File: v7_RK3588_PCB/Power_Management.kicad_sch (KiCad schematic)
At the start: 0 parts

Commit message: add symbols
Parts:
- added U3001: ~, RK806-1:QFN-68_L7.0-W7.0-P0.35-BL-EP5.5, symbol RK806-1:RK806-1_C5156483

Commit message: add regulators
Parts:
- added C3001, C3012, C3013: 47u, symbol Device:C
- added C3002, C3003: 22u, symbol Device:C
- added C3004, C3005: 10u, symbol Device:C
- added C3006, C3014: 100n, symbol Device:C
- added C3007, C3008: 1u, symbol Device:C
- added C3009: 47p, symbol Device:C
- added C3010: 1n, symbol Device:C
- added C3011: 8.2n, symbol Device:C
- added L3001: 220n, symbol Device:L
- added L3002: 1u, symbol Device:L
- added R3001: 100k, symbol Device:R
- added R3002: 205k, symbol Device:R
- added R3003: 23.7k, symbol Device:R
- added R3004: 124k, symbol Device:R
- added R3005: 267k, symbol Device:R
- added R3006: 220k, symbol Device:R
- added R3007: 69.8k, symbol Device:R
- added U3002: TPS62867RQYR, TPS62867RQYR:RQY0009A-MFG, symbol TPS62867RQYR:TPS62867RQYR
- added U3003: TPS61088RHLR, TPS61088RHLR:IC_TPS61088RHLR, symbol TPS61088RHLR:TPS61088RHLR
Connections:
- new net: C3004.1, C3005.1, C3006.1, L3002.1, U3003.9 (VIN)
- new net: R3006.2, R3007.1, U3003.17 (FB)
- new net: C3007.1, C3008.1, U3003.1 (VCC)
- new net: C3014.2, L3002.2, R3005.1, U3003.4 (SW_7), U3003.5 (SW_4), U3003.6 (SW_5), U3003.7 (SW_6)
- new net: R3005.2, U3003.3 (FSW)
- new net: C3009.1, R3003.1, U3003.18 (COMP)
- new net: R3002.1, U3002.6 (VSET_MODE)
- new net: C3014.1, U3003.8 (BOOT)
- new net: L3001.1, U3002.7 (SW)
- new net: C3010.1, R3003.2
- new net: R3004.1, U3003.19 (ILIM)
- new net: C3011.1, U3003.10 (SS)
- new net 5V0_OUT_ETH: C3001.1, R3001.1, U3002.3 (VIN), U3002.4 (EN)
- new net BAT_5V: C3012.1, C3013.1, R3006.1, U3003.14 (VOUT_16), U3003.15 (VOUT_14), U3003.16 (VOUT_15)
- new net ETH_3V3: C3002.1, C3003.1, L3001.2, U3002.8 (VOS), U3002.9 (FB)
- new net ETH_3V3_PG: R3001.2, U3002.5 (PG)
- new net GND: C3001.2, C3002.2, C3003.2, C3004.2, C3005.2, C3006.2, C3007.2, C3008.2, C3009.2, C3010.2, C3011.2, C3012.2, C3013.2, R3002.2, R3004.2, R3007.2, U3002.1 (AGND), U3002.2 (PGND), U3003.11 (NC_11), U3003.20 (AGND), U3003.21 (PGND), U3003.22 (PGND__1), U3003.23 (PGND__2), U3003.24 (PGND__3), U3003.25 (PGND__4), U3003.26 (PGND__5), U3003.27 (PGND__6), U3003.28 (PGND__7), U3003.29 (PGND__8)
- no-connect marks 0 -> 1
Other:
- note added: "Battery to 5V"
- note added: "CONNECT TO IDEAL DIODE PG"
- note added: "PoE to 3.3V"
- note added: "SEE PG 12 OF DATASHEET FOR CAP. VALUE CALC"
- note added: "USE PG TO DISABLE BATTERY 3V3 REG"
- moved on the sheet: U3001

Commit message: add battery management
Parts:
- added BT3001, BT3002: Battery_Cell, symbol Device:Battery_Cell
- added C3015, C3016, C3017, C3018: 0.1u, symbol Device:C
- added C3019, C3020: 4.3n, symbol Device:C
- added R3008, R3015: 470k, symbol Device:R
- added R3009, R3017: 118k, symbol Device:R
- added R3010, R3020: 215k, symbol Device:R
- added R3011, R3021: 576, symbol Device:R
- added R3012, R3016: 47k, symbol Device:R
- added R3013, R3018: 27.4k, symbol Device:R
- added R3014, R3019: 10k, symbol Device:R
- added U3004, U3005: LTC4450AV-TRMPBF, LTC4450:05-08-1683_ADI, symbol LTC4450:LTC4450AV-TRMPBF
- added U3006, U3007: TPS22811LRPWR, TPS22811LRPWR:IC_TPS22811LRPWR, symbol TPS22811LRPWR:TPS22811LRPWR
- added U3008: SN74AHC1G32DCKR, SN74AHC1G32DCKR:SOT65P210X110-5N, symbol SN74AHC1G32DCKR:SN74AHC1G32DCKR
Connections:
- net GND: now also BT3001.2 (-), BT3002.2 (-), C3015.2, C3016.2, C3017.2, C3018.2, C3019.2, C3020.2, R3010.2, R3011.2, R3013.2, R3018.2, R3020.2, R3021.2, U3004.1 (VCC), U3004.14 (GND), U3004.15 (STATUS), U3005.1 (VCC), U3005.14 (GND), U3005.15 (STATUS), U3006.8 (GND), U3007.8 (GND), U3008.3 (GND)
- new net: BT3001.1 (+), R3008.1, U3006.5 (IN)
- new net: R3008.2, R3009.1, U3006.1 (EN/UVLO)
- new net: BT3002.1 (+), R3015.1, U3007.5 (IN)
- new net: R3015.2, R3017.1, U3007.1 (EN/UVLO)
- new net: R3009.2, R3010.1, U3006.2 (~{EN}/OVLO)
- new net: R3016.2, R3018.1, U3007.4 (PGTH)
- new net: R3021.1, U3007.9 (IMON)
- new net: C3019.1, U3006.7 (DVDT)
- new net: R3017.2, R3020.1, U3007.2 (~{EN}/OVLO)
- new net: C3020.1, U3007.7 (DVDT)
- new net: R3012.2, R3013.1, U3006.4 (PGTH)
- new net: R3011.1, U3006.9 (IMON)
- new net BATTERY_IN: C3016.1, C3018.1, U3004.10 (OUT), U3004.11 (OUT), U3004.12 (OUT), U3004.13 (OUT), U3004.8 (OUT), U3004.9 (OUT), U3005.10 (OUT), U3005.11 (OUT), U3005.12 (OUT), U3005.13 (OUT), U3005.8 (OUT), U3005.9 (OUT), U3008.5 (VCC)
- new net BATTERY_PG: U3008.4 (Y)
- new net LOAD_OUT_1: C3015.1, R3012.1, U3004.16 (SHDN#), U3004.2 (IN), U3004.3 (IN), U3004.4 (IN), U3004.5 (IN), U3004.6 (IN), U3004.7 (IN), U3006.6 (OUT)
- new net LOAD_OUT_2: C3017.1, R3016.1, U3005.16 (SHDN#), U3005.2 (IN), U3005.3 (IN), U3005.4 (IN), U3005.5 (IN), U3005.6 (IN), U3005.7 (IN), U3007.6 (OUT)
- new net LOAD_PG_1: R3014.2, U3006.3 (PG), U3008.1 (A)
- new net LOAD_PG_2: R3019.2, U3007.3 (PG), U3008.2 (B)
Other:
- note added: "Battery Management"
- note added: "CONNECT TO LOAD SWITCH PG"
- note added: "POSSIBLY ADD INPUT TVS DIODES"
- note added: "STATUS indication unused"
- note added: "TODO: Pull up"
- note added: "TODO: pick and insert fuel gauge"
- note removed: "CONNECT TO IDEAL DIODE PG"
- moved on the sheet: C3001, C3002, C3003, C3004, C3005, C3006, C3007, C3008, C3009, C3010, C3011, C3012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

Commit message: add ESP32 schematic
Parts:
- added R3022: 10k, symbol Device:R
- renumbered C3002 to C3001, C3003 to C3002, C3001 to C3003, C3014 to C3004, C3015 to C3005, C3016 to C3006, C3004 to C3007, C3005 to C3008, C3006 to C3009, C3007 to C3010, C3008 to C3011, C3019 to C3012, C3012 to C3013, C3013 to C3014, C3009 to C3015, C3010 to C3016, C3011 to C3019, R3005 to R3003, R3008 to R3004, R3012 to R3005, R3009 to R3006, R3013 to R3007, R3014 to R3008, R3010 to R3009, R3011 to R3010, R3006 to R3011, R3003 to R3012, R3007 to R3013, R3004 to R3014, U3002 to U3001, U3004 to U3002, U3006 to U3003, U3003 to U3004, U3007 to U3006, U3008 to U3007, U3001 to U3008
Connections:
- net BATTERY_PG: now also U3004.2 (EN)
- net GND: now also U3008.69 (PAD)
- net PMIC_INT_L: now reaches U3008.19 (INT)
- net PMIC_INT_L: now also R3022.2
- net PMIC_EXT_EN_OUT: now reaches U3008.39 (EXT_EN)
- net RESET_L: now reaches U3008.40 (RESETB)
- net PMIC_PWR_CTRL2: now reaches U3008.61 (PWRCRTL2)
- net PMIC_PWR_CTRL1: now reaches U3008.62 (PWRCRTL1)
- new net VCC_1V8_S3: R3022.1
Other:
- note added: "TODO: add another protection IC?"
- note removed: "CONNECT TO LOAD SWITCH PG"
- moved on the sheet: C3004, C3005, C3006, C3007, C3008, C3009, C3010, C3011, C3012, C3013, C3014, C3015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

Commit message: add power sequencing
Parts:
- removed U3007: SN74AHC1G32DCKR, SN74AHC1G32DCKR:SOT65P210X110-5N, symbol SN74AHC1G32DCKR:SN74AHC1G32DCKR
- added C3021, C3022, C3023, C3024, C3025: 0.1u, symbol Device:C
- added R3023, R3024, R3029, R3030: 100, symbol Device:R
- added R3025: 1m, symbol Device:R
- added R3026: 10, symbol Device:R
- added R3027, R3028: 1k, symbol Device:R
- added TH3001: ERT-J0EG103FA, symbol Device:Thermistor
- added U3004: BQ27Z561YPHR-R2, BQ27Z561-R2:DSBGA_YPHR-R2_TEX, symbol BQ27Z561-R2:BQ27Z561YPHR-R2
- added U3008: SN74LVC1G32DBVR, SN74LVC1G32DBVR:SOT95P280X145-5N, symbol SN74LVC1G32DBVR:SN74LVC1G32DBVR
- added U3010: LTC4450AV-TRMPBF, LTC4450:05-08-1683_ADI, symbol LTC4450:LTC4450AV-TRMPBF
- added U3011: SN74LVC1G14DBVR, SN74LVC1G14DBVR:SOT95P280X145-5N, symbol SN74LVC1G14DBVR:SN74LVC1G14DBVR
- added U3012: SN74LVC1G08DBVR, SN74LVC1G08DBVR:SOT95P280X145-5N, symbol SN74LVC1G08DBVR:SN74LVC1G08DBVR
- R3006, R3017: value 118k -> 82.5k
- R3009, R3020: value 215k -> 205k
- renumbered U3004 to U3005, U3005 to U3006, U3006 to U3007, U3008 to U3009
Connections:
- net BATTERY_IN: now also C3021.1, R3024.1, R3025.2, R3026.2, R3027.2, R3028.2, U3008.5 (VCC)
- net BATTERY_PG: now also U3008.4, U3012.2 (B)
- net ETH_3V3: now also C3024.1, U3010.16 (SHDN#), U3010.2 (IN), U3010.3 (IN), U3010.4 (IN), U3010.5 (IN), U3010.6 (IN), U3010.7 (IN)
- net ETH_3V3_PG: now also U3011.2 (A)
- net GND: now also C3021.2, C3022.2, C3024.2, C3025.2, TH3001.2, U3004.B2 (VSS), U3008.3 (GND), U3010.1 (VCC), U3010.14 (GND), U3010.15 (STATUS), U3011.3 (GND), U3012.3 (GND)
- net LOAD_PG_1: now also U3008.1
- net LOAD_PG_2: now also U3008.2
- net BATTERY_PACK_OUT: now reaches C3007.1, C3008.1, C3009.1, L3002.1, U3005.9 (VIN)
- net BATTERY_PACK_OUT: now also R3023.1, R3025.1
- new net: R3027.1, U3004.D3 (CE)
- new net: C3022.1, TH3001.1, U3004.B1 (TS)
- new net: C3023.1, R3023.2, U3004.D1 (SRP)
- new net: C3023.2, R3024.2, U3004.C1 (SRN)
- new net: C3025.1, U3010.10 (OUT), U3010.11 (OUT), U3010.12 (OUT), U3010.13 (OUT), U3010.8 (OUT), U3010.9 (OUT)
- new net: R3026.1, U3004.D2 (BAT)
- new net: R3028.1, U3004.C2 (BAT_SNS)
- new net: U3011.4 (Y), U3012.1 (A)
- new net: R3030.1, U3004.B3 (SCL)
- new net: R3029.1, U3004.A3 (SDA/HDQ)
- new net BAT_3V3_EN: U3012.4 (Y)
- new net FUEL_GAUGE_INT: U3004.A1 (INT)
- new net FUEL_GAUGE_PULS: U3004.A2 (PULS)
- new net FUEL_GAUGE_SCL: R3030.2
- new net FUEL_GAUGE_SDA: R3029.2
- new net VCC3V3_SYS: U3011.5 (VCC), U3012.5 (VCC)
- no-connect marks 1 -> 2
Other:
- note added: "5V Boost EN when good battery"
- note added: "Battery 3.3V Buck EN when good battery and no POE"
- note added: "NOTE: BAT_SNS must tie to positive battery pack terminal on independent path from BAT pin"
- note added: "Power Sequencing/EN Logic"
- note added: "TODO: expose I2C connection for firmware flash? or connect to MCU/SoC? TODO: pullups"
- note removed: "TODO: add another protection IC?"
- note removed: "TODO: pick and insert fuel gauge"
- note removed: "USE PG TO DISABLE BATTERY 3V3 REG"
- moved on the sheet: C3004, C3005, C3006, C3007, C3008, C3009, C3010, C3011, C3012, C3013, C3014, C3015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

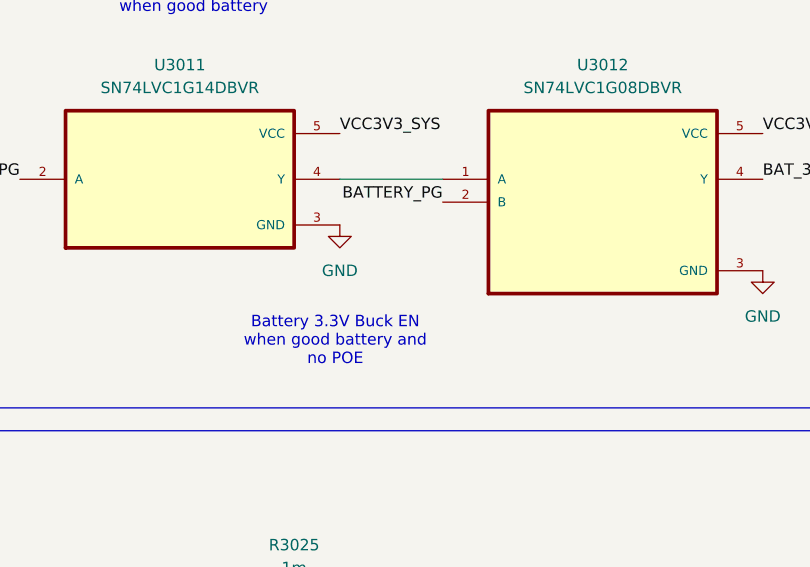
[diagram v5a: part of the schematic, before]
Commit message: add WiFi module
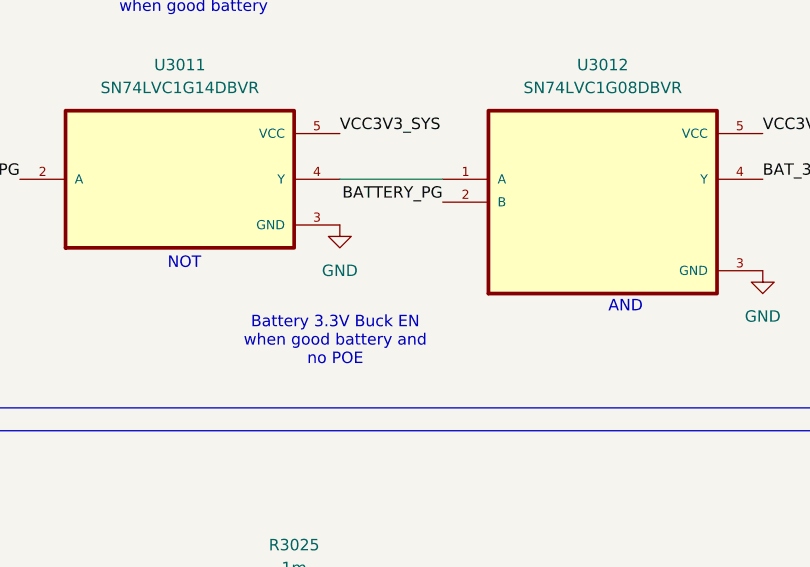
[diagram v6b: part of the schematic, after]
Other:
- note added: "AND"
- note added: "NOT"
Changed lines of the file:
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@@
+		)
+	)
+	(text "AND"
+		(exclude_from_sim no)
+		(at 360.68 95.504 0)
+		(effects
+			(font
+				(size 1.27 1.27)
+			)
 		)
 	)
@@
 		(effects
 			(font
+				(size 1.27 1.27)
+			)
+		)
+	)
+	(text "NOT"
+		(exclude_from_sim no)
+		(at 311.658 90.678 0)
+		(effects
+			(font

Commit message: add 5V power mux
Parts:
- added C?: 100nF, symbol Device:C
- added D3001, D3002: D_TVS, ESD5451N2:DFN1006-2L_TWS, symbol Device:D_TVS
- added R? (x3): 0, symbol Device:R
- added R? (x2): 5k, symbol Device:R
- added R?: 8.2k, symbol Device:R
- added R?: 10k, symbol Device:R
- added R?: 24k, symbol Device:R
- added U3013: TPS2121RUXR, RUX0012A, symbol TPS2121RUXR:TPS2121RUXR
- C3019: value 8.2n -> 47u
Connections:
- net 5V0_OUT_ETH: now also R?.1, R?.2
- net BAT_5V: now also R?.1, R?.1
- net GND: now also C?.2, D3001.1 (A1), D3002.1 (A1), R?.1, R?.2, R?.2, U3013.12 (GND), U3013.4 (OV2), U3013.5 (OV1)
- net LOAD_OUT_1: now also R3008.1, D3001.2 (A2)
- net LOAD_OUT_2: now also R3019.1, D3002.2 (A2)
- new net: R?.2, U3013.2 (IN2)
- new net: R?.1, U3013.1 (OUT), U3013.8 (OUT)
- new net: R?.1, U3013.10 (ILM)
- new net: C?.1, U3013.11 (SS)
- new net: R?.2, U3013.7 (IN1)
- new net 5V_MUX_STATUS: U3013.9 (ST)
- new net CP2: R?.2, R?.2, U3013.3 (CP2)
- new net PR1: R?.1, R?.1, U3013.6 (PR1)
- new net VCC5V_SYS: R?.2
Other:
- note added: "Battery/Ethernet 5V Switchover"
- note removed: "POSSIBLY ADD INPUT TVS DIODES"
- note removed: "SEE PG 12 OF DATASHEET FOR CAP. VALUE CALC"
- note removed: "TODO: Pull up"
- moved on the sheet: C3004, C3007, C3008, C3009, C3010, C3011, C3013, C3014, C3015, C3016, C3019, L3002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

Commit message: add battery 3v3 regulator
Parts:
- added C3026: 330u, symbol Device:C
- added C3027: 10u, symbol Device:C
- added C3028, C3034: 1u, symbol Device:C
- added C3029: 4.7u, symbol Device:C
- added C3030: 150p, symbol Device:C
- added C3031: 18n, symbol Device:C
- added C3032, C3033: 100n, symbol Device:C
- added C3035, C3036, C3037: 47u, symbol Device:C
- added C3038: 560u, symbol Device:C
- added C3039: 0.1u, symbol Device:C
- added L3003: 4.7u, symbol Device:L
- added R3031: 162k, symbol Device:R
- added R3032: 100k, symbol Device:R
- added R3033: 24.9k, symbol Device:R
- added R3034: 12.1k, symbol Device:R
- added R3035: 102k, symbol Device:R
- added R3036: 9.53k, symbol Device:R
- added U3014: XTPS55285VALR, TPS55285VALR:VAL0015A, symbol TPS55285VALR:XTPS55285VALR
- added U3015: LTC4450AV-TRMPBF, LTC4450:05-08-1683_ADI, symbol LTC4450:LTC4450AV-TRMPBF
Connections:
- net BATTERY_PACK_OUT: now also C3026.1, C3027.1, C3028.1, U3014.5 (VIN)
- net BAT_3V3_EN: now also R3031.1
- net GND: now also C3026.2, C3027.2, C3028.2, C3029.2, C3030.2, C3031.2, C3034.2, C3035.2, C3036.2, C3037.2, C3038.2, C3039.2, R3032.2, R3033.1, R3036.1, U3014.12 (AGND), U3014.7 (PGND), U3015.1 (VCC), U3015.14 (GND), U3015.15 (STATUS)
- net VCC3V3_SYS: now also C3025.1, U3010.10 (OUT), U3010.11 (OUT), U3010.12 (OUT), U3010.13 (OUT), U3010.8 (OUT), U3010.9 (OUT), C3039.1, U3015.10 (OUT), U3015.11 (OUT), U3015.12 (OUT), U3015.13 (OUT), U3015.8 (OUT), U3015.9 (OUT)
- new net: C3034.1, C3035.1, C3036.1, C3037.1, C3038.1, R3035.2, U3014.9 (VOUT), U3015.16 (SHDN#), U3015.2 (IN), U3015.3 (IN), U3015.4 (IN), U3015.5 (IN), U3015.6 (IN), U3015.7 (IN)
- new net: R3033.2, U3014.1 (MODE)
- new net: R3031.2, R3032.1, U3014.4 (EN_UVLO)
- new net: C3029.1, U3014.13 (VCC)
- new net: C3030.1, R3034.2, U3014.11 (COMP)
- new net: R3035.1, R3036.2, U3014.10 (FB_INT_N)
- new net: C3031.1, R3034.1
- new net: C3033.1, L3003.2, U3014.8 (SW2)
- new net: C3033.2, U3014.14 (BOOT2)
- new net: C3032.2, U3014.15 (BOOT1)
- new net: C3032.1, L3003.1, U3014.6 (SW1)
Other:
- note added: "Battery to 3.3V"
